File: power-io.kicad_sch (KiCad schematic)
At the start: 13 parts, among them J1 USB4105-GF-A, J2 J2 GPIO / 2.00mm, J3 J3 GPIO / 2.00mm, U2 AP2112K-3.3

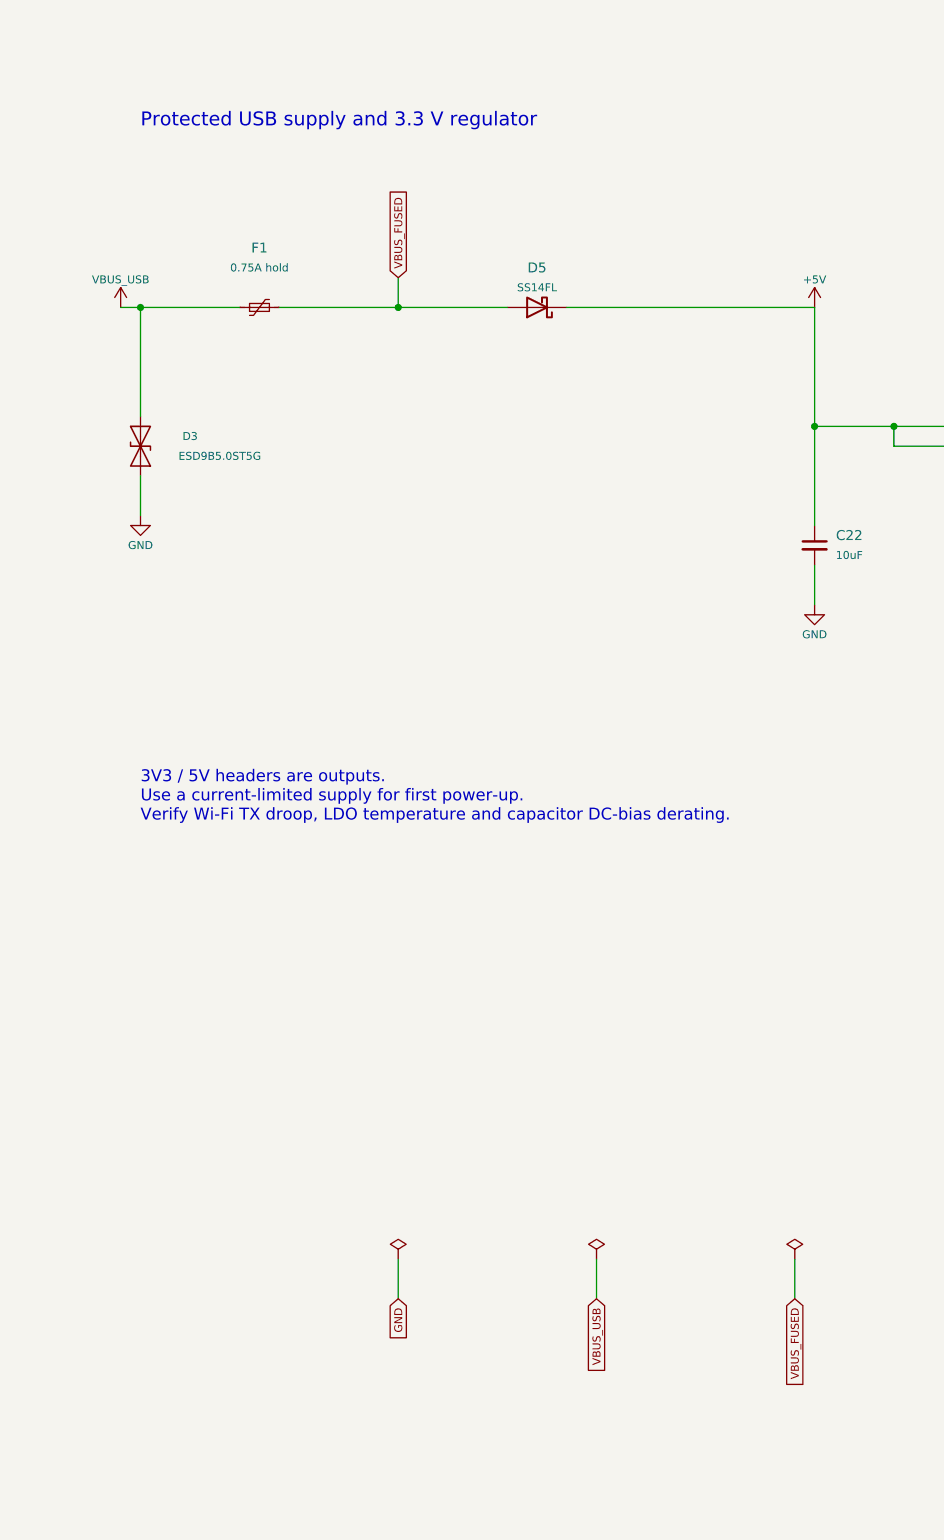
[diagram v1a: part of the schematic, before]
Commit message: Restore SOIC-8 flash, shrink USB diode and remove input fuse
Use W25Q32JVSNIQ in a 150 mil SOIC-8 footprint and BAT760-7 in
SOD-323. Remove F1 and connect USB VBUS directly to the blocking
diode. Preserve the board outline and RF, crystal and USB data routing.

Synchronize schematics, BOM, placement, previews, fabrication notes and
independent checks. ERC, DRC, unconnected items and schematic parity
are all zero. QA passes 45 of 51 checks, retaining six pre-existing failures.
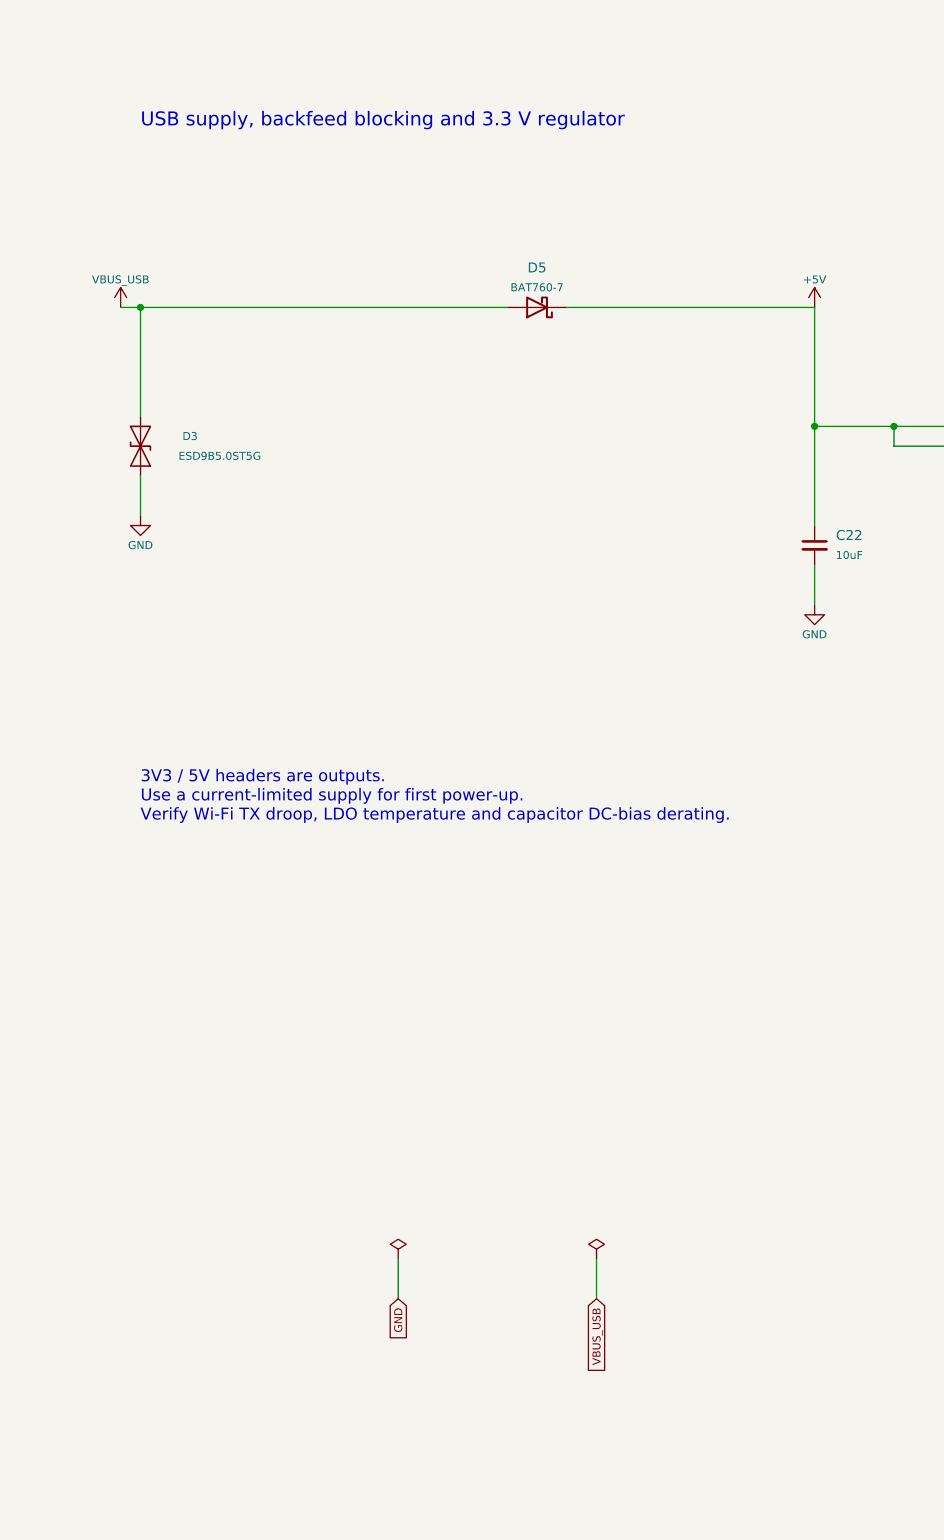
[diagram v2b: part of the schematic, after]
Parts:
- removed F1: 0.75A hold, Fuse:Fuse_1206_3216Metric, symbol Pico_Design:Device__Polyfuse_Small
- D5: value SS14FL -> BAT760-7; footprint Diode_SMD:D_SOD-123F -> Diode_SMD:D_SOD-323; AssemblyNote Blocks USB backfeed; +5V is about VBUS minus diode drop -> Same part/package as at820_tiga D9/D10; 30 V, 1 A with data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; MPN SS14FL -> BAT760-7
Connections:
- net VBUS_FUSED is gone; now on net VBUS_USB: D5.2 (A)
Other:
- note added: "USB supply, backfeed blocking and 3.3 V regulator"
- note removed: "Protected USB supply and 3.3 V regulator"
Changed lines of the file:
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@@
 		)
 	)
-	(text "Protected USB supply and 3.3 V regulator"
+	(text "USB supply, backfeed blocking and 3.3 V regulator"
 		(at 220.98 30.48 0)
 		(effects
@@
 			)
 			(justify left bottom)
-		)
-	)
-	(symbol
-		(lib_id "Pico_Design:Device__Polyfuse_Small")
-		(at 236.22 53.34 90)
-		(unit 1)
-		(in_bom yes)
-		(on_board yes)
-		(dnp no)
-		(property "Reference" "F1"
-			(at 236.22 45.72 90)
-			(effects
-				(font
-					(size 1.27 1.27)
-				)
-			)
-		)
-		(property "Value" "0.75A hold"
-			(at 236.22 48.26 90)
-			(effects
-				(font
-					(size 1.016 1.016)
-				)
-			)
-		)
-		(property "Footprint" "Fuse:Fuse_1206_3216Metric"
-			(at 236.22 53.34 0)
-			(effects
-				(font
-					(size 0.9 0.9)
-				)
-				(hide yes)
-			)
-		)
-		(property "Datasheet" ""
-			(at 236.22 53.34 0)
-			(effects
-				(font
-					(size 0.9 0.9)
-				)
-				(hide yes)
-			)
-		)
-		(property "MPN" "1206L075/6"
-			(at 236.22 53.34 0)
-			(effects
-				(font
-					(size 0.9 0.9)
-				)
-				(hide yes)
-			)
-		)
-		(property "AssemblyNote" "Check thermal derating; input source >=500 mA"
-			(at 236.22 53.34 0)
-			(effects
-				(font
-					(size 0.9 0.9)
-				)
-				(hide yes)
-			)
-		)
-		(pin "1"
-		)
-		(pin "2"
-		)
-		(instances
-			(project "esp32-c6-pico"
-				(path "/d29d372c-7a4c-447f-ba6c-21fb60482be4/13033aea-e4f8-548e-9e40-21ec019685cb"
-					(reference "F1")
-					(unit 1)
-				)
-			)
 		)
 	)
@@
 			)
 		)
-		(property "Value" "SS14FL"
+		(property "Value" "BAT760-7"
 			(at 271.78 50.8 0)
 			(effects
@@
 			)
 		)
-		(property "Footprint" "Diode_SMD:D_SOD-123F"
+		(property "Footprint" "Diode_SMD:D_SOD-323"
 			(at 271.78 53.34 0)
 			(effects
@@
 			)
 		)
-		(property "Datasheet" "https://www.onsemi.com/download/data-sheet/pdf/ss14fl-d.pdf"
+		(property "Datasheet" "https://www.diodes.com/datasheet/download/BAT760.pdf"
 			(at 271.78 53.34 0)
 			(effects
@@
 			)
 		)
-		(property "MPN" "SS14FL"
+		(property "MPN" "BAT760-7"
 			(at 271.78 53.34 0)
 			(effects
@@
 			)
 		)
-		(property "AssemblyNote" "Blocks USB backfeed; +5V is about VBUS minus diode drop"
+		(property "AssemblyNote" "Same part/package as at820_tiga D9/D10; 30 V, 1 A with datasheet thermal derating; blocks USB backfeed"
 			(at 271.78 53.34 0)
 			(effects
@@
 		)
 	)
-	(global_label "VBUS_FUSED"
-		(shape input)
-		(at 254.0 49.53 90)
-		(effects
-			(font
-				(size 1.016 1.016)
-			)
-			(justify left)
-		)
-		(property "Intersheetrefs" "${INTERSHEET_REFS}"
-			(at 254.0 49.53 90)
-			(effects
-				(font
-					(size 1 1)
-				)
-				(hide yes)
-			)
-		)
-	)
 	(symbol
 		(lib_id "Pico_Design:power__+3V3")
@@
 	(symbol
 		(lib_id "Pico_Design:power__PWR_FLAG")
-		(at 304.8 175.26 0)
-		(unit 1)
-		(in_bom no)
-		(on_board no)
-		(dnp no)
-		(property "Reference" "#FLG02"
-			(at 304.8 170.18 0)
-			(effects
-				(font
-					(size 1.27 1.27)
-				)
-				(hide yes)
-			)
-		)
-		(property "Value" "PWR_FLAG"
-			(at 304.8 172.72 0)
-			(effects
-				(font
-					(size 1.016 1.016)
-				)
-				(hide yes)
-			)
-		)
-		(property "Footprint" ""
-			(at 304.8 175.26 0)
-			(effects
-				(font
-					(size 0.9 0.9)
-				)
-				(hide yes)
-			)
-		)
-		(property "Datasheet" ""
-			(at 304.8 175.26 0)
-			(effects
-				(font
-					(size 0.9 0.9)
-				)
-				(hide yes)
-			)
-		)
-		(property "MPN" "PWR_FLAG"
-			(at 304.8 175.26 0)
-			(effects
-				(font
-					(size 0.9 0.9)
-				)
-				(hide yes)
-			)
-		)
-		(property "AssemblyNote" ""
-			(at 304.8 175.26 0)
-			(effects
-				(font
-					(size 0.9 0.9)
-				)
-				(hide yes)
-			)
-		)
-		(pin "1"
-		)
-		(instances
-			(project "esp32-c6-pico"
-				(path "/d29d372c-7a4c-447f-ba6c-21fb60482be4/13033aea-e4f8-548e-9e40-21ec019685cb"
-					(reference "#FLG02")
-					(unit 1)
-				)
-			)
-		)
-	)
-	(global_label "VBUS_FUSED"
-		(shape input)
-		(at 304.8 180.34 270)
-		(effects
-			(font
-				(size 1.016 1.016)
-			)
-			(justify right)
-		)
-		(property "Intersheetrefs" "${INTERSHEET_REFS}"
-			(at 304.8 180.34 270)
-			(effects
-				(font
-					(size 1 1)
-				)
-				(hide yes)
-			)
-		)
-	)
-	(symbol
-		(lib_id "Pico_Design:power__PWR_FLAG")
 		(at 330.2 175.26 0)
 		(unit 1)
@@
 	(wire
 		(pts
-			(xy 238.76 53.34)
-			(xy 254.0 53.34)
-		)
-		(stroke
-			(width 0)
-			(type default)
-		)
-	)
-	(wire
-		(pts
-			(xy 254.0 49.53)
-			(xy 254.0 53.34)
-		)
-		(stroke
-			(width 0)
-			(type default)
-		)
-	)
-	(wire
-		(pts
-			(xy 254.0 53.34)
-			(xy 267.97 53.34)
-		)
-		(stroke
-			(width 0)
-			(type default)
-		)
-	)
-	(wire
-		(pts
-			(xy 304.8 175.26)
-			(xy 304.8 180.34)
-		)
-		(stroke
-			(width 0)
-			(type default)
-		)
-	)
-	(wire
-		(pts
 			(xy 60.96 69.85)
 			(xy 66.04 69.85)
@@
 		(pts
 			(xy 220.98 53.34)
-			(xy 233.68 53.34)
+			(xy 267.97 53.34)
 		)
 		(stroke
@@
 		(diameter 0)
 		(color 0 0 0 0)
-	)
-	(junction
-		(at 254.0 53.34)
-		(diameter 0)
-		(color 0 0 0 0)

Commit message: Complete first PCB revision
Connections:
- net GPIO8 is gone; now on net +3V3: J2.11 (Pin_11)
- net +3V3: no longer J2.2 (Pin_2)
- net +5V: now also J3.11 (Pin_11); no longer J3.1 (Pin_1)
- net GND: now also J2.12 (Pin_12), J3.12 (Pin_12); no longer J2.1 (Pin_1), J3.2 (Pin_2)
- net GPIO0: now also J3.1 (Pin_1); no longer J2.3 (Pin_3)
- net GPIO1: now also J2.1 (Pin_1); no longer J2.4 (Pin_4)
- net GPIO10: now also J2.9 (Pin_9); no longer J3.3 (Pin_3)
- net GPIO11: now also J2.10 (Pin_10); no longer J3.4 (Pin_4)
- net GPIO15: now also J3.10 (Pin_10); no longer J3.5 (Pin_5)
- net GPIO18: now also J3.7 (Pin_7); no longer J3.8 (Pin_8)
- net GPIO19: now also J3.6 (Pin_6); no longer J3.9 (Pin_9)
- net GPIO2: now also J2.2 (Pin_2); no longer J2.5 (Pin_5)
- net GPIO20: now also J3.5 (Pin_5); no longer J3.10 (Pin_10)
- net GPIO22: now also J3.3 (Pin_3); no longer J3.11 (Pin_11)
- net GPIO23: now also J3.2 (Pin_2); no longer J3.12 (Pin_12)
- net GPIO3: now also J2.3 (Pin_3); no longer J2.6 (Pin_6)
- net GPIO4: now also J2.4 (Pin_4); no longer J2.7 (Pin_7)
- net GPIO5: now also J2.5 (Pin_5); no longer J2.8 (Pin_8)
- net GPIO6: now also J2.6 (Pin_6); no longer J2.9 (Pin_9)
- net GPIO7: now also J2.7 (Pin_7); no longer J2.10 (Pin_10)
- net GPIO9_BOOT: now also J2.8 (Pin_8); no longer J2.12 (Pin_12)
- net U0RXD: now also J3.9 (Pin_9); no longer J3.7 (Pin_7)
- net U0TXD: now also J3.8 (Pin_8); no longer J3.6 (Pin_6)
- new net GPIO21: J3.4 (Pin_4)
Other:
- moved on the sheet: J3
